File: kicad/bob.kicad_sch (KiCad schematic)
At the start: 53 parts, among them J1 Mini USB Female, J2 GPIO (Optional), J3 GPIO (Optional), J4 Battery Connector, J5 Conn_01x03_Male, SW1 Screw Switch, U1 W25Q64JVSS, U2 AMS1117-3.3, U3 RP2040, Y1 12MHz

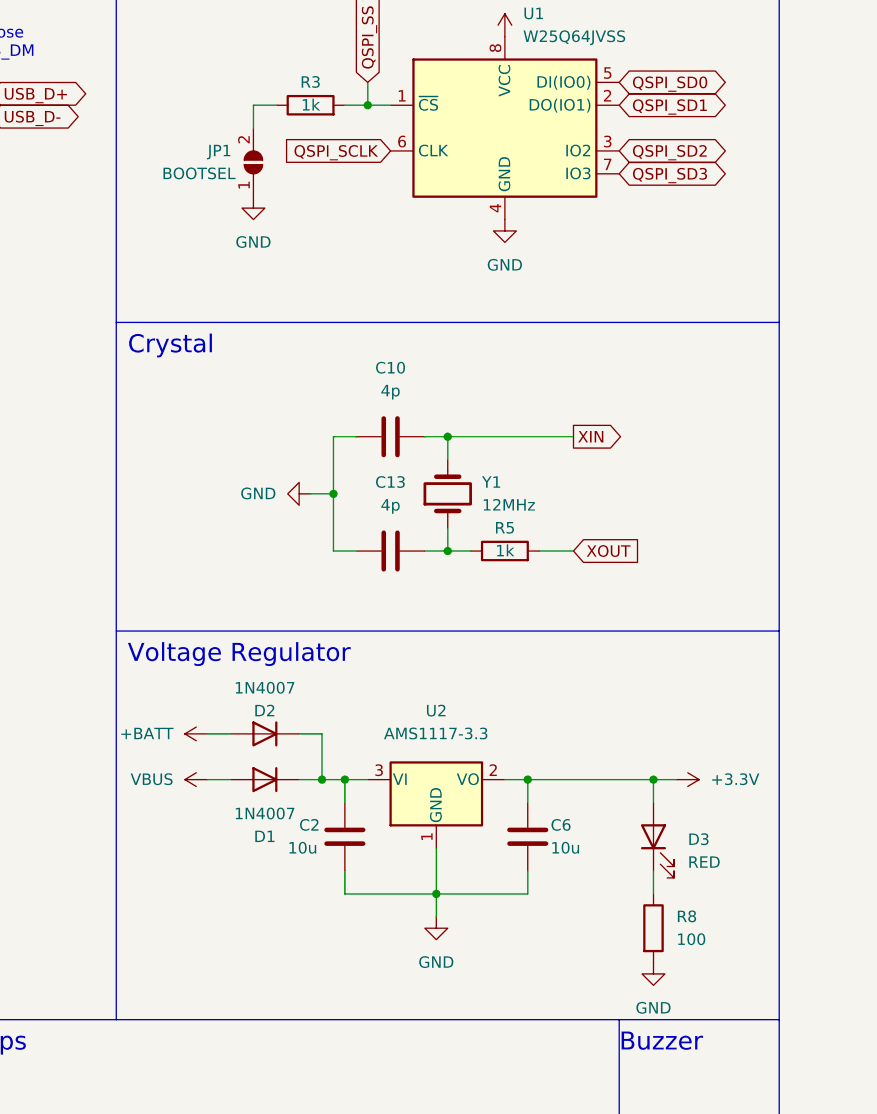
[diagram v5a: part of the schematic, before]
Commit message: Changed LED current limiter so it wont be so bright
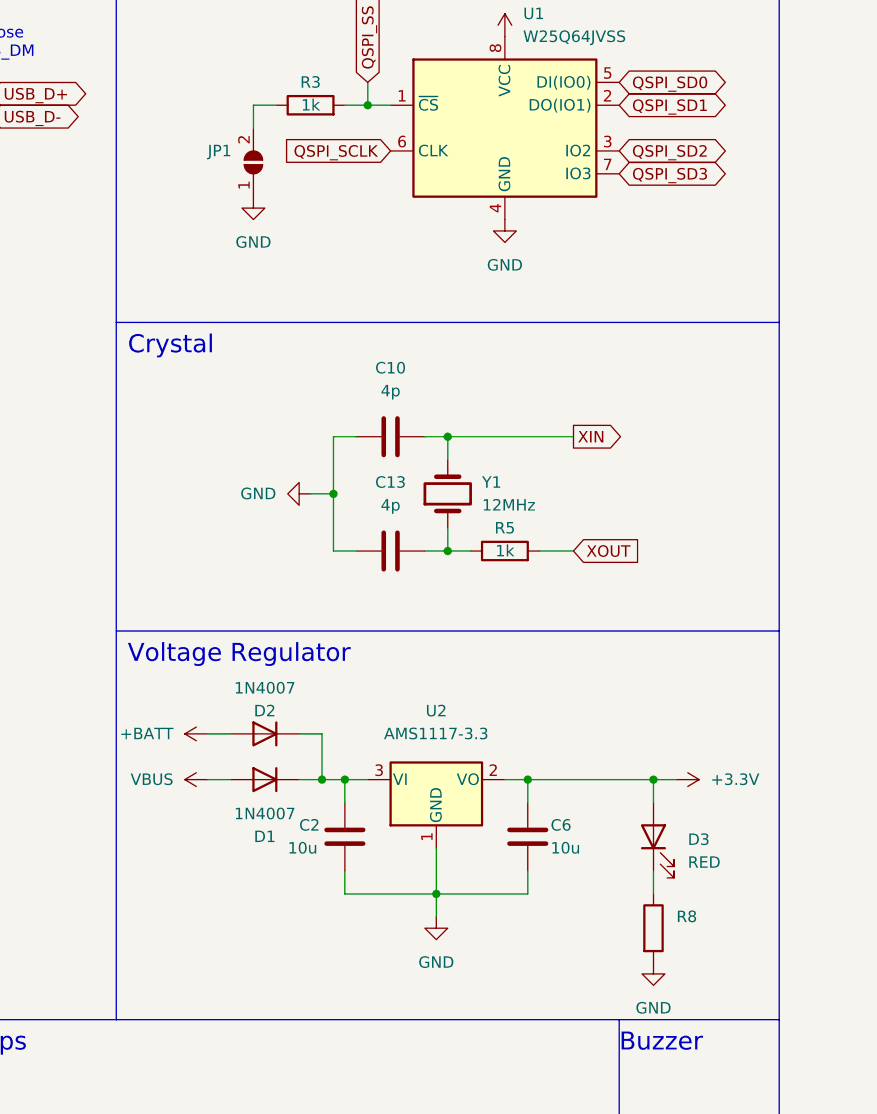
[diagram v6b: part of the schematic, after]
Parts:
- JP1: value BOOTSEL -> (none); footprint Jumper:SolderJumper-2_P1.3mm_Open_RoundedPad1.0x1.5mm -> (none)
- R8: value 100 -> (none)
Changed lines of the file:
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@@
   (symbol (lib_id "power:+3.3V") (at 247.65 27.94 0) (unit 1)
     (in_bom yes) (on_board yes) (fields_autoplaced)
-    (property "Reference" "#PWR?" (id 0) (at 247.65 31.75 0)
+    (property "Reference" "#PWR0106" (id 0) (at 247.65 31.75 0)
       (effects (font (size 1.27 1.27)) hide)
     )
@@
   (symbol (lib_id "power:GND") (at 261.62 40.64 90) (unit 1)
     (in_bom yes) (on_board yes) (fields_autoplaced)
-    (property "Reference" "#PWR?" (id 0) (at 267.97 40.64 0)
+    (property "Reference" "#PWR0149" (id 0) (at 267.97 40.64 0)
       (effects (font (size 1.27 1.27)) hide)
     )
@@
   (symbol (lib_id "power:+3.3V") (at 233.68 35.56 90) (unit 1)
     (in_bom yes) (on_board yes)
-    (property "Reference" "#PWR?" (id 0) (at 237.49 35.56 0)
+    (property "Reference" "#PWR0129" (id 0) (at 237.49 35.56 0)
       (effects (font (size 1.27 1.27)) hide)
     )
@@
   (symbol (lib_id "power:GND") (at 247.65 58.42 0) (unit 1)
     (in_bom yes) (on_board yes) (fields_autoplaced)
-    (property "Reference" "#PWR?" (id 0) (at 247.65 64.77 0)
+    (property "Reference" "#PWR0130" (id 0) (at 247.65 64.77 0)
       (effects (font (size 1.27 1.27)) hide)
     )
@@
       (effects (font (size 1.27 1.27)) (justify left))
     )
-    (property "Value" "100" (id 1) (at 184.15 126.9999 0)
+    (property "Value" "" (id 1) (at 184.15 126.9999 0)
       (effects (font (size 1.27 1.27)) (justify left))
     )
@@
   (symbol (lib_id "power:GND") (at 233.68 43.18 270) (unit 1)
     (in_bom yes) (on_board yes) (fields_autoplaced)
-    (property "Reference" "#PWR?" (id 0) (at 227.33 43.18 0)
+    (property "Reference" "#PWR0107" (id 0) (at 227.33 43.18 0)
       (effects (font (size 1.27 1.27)) hide)
     )
@@
       (effects (font (size 1.27 1.27)) (justify right))
     )
-    (property "Value" "BOOTSEL" (id 1) (at 127 41.91 90)
+    (property "Value" "" (id 1) (at 127 41.91 90)
       (effects (font (size 1.27 1.27)) (justify right))
     )
-    (property "Footprint" "Jumper:SolderJumper-2_P1.3mm_Open_RoundedPad1.0x1.5mm" (id 2) (at 137.16 40.64 0)
+    (property "Footprint" "" (id 2) (at 137.16 40.64 0)
       (effects (font (size 1.27 1.27)) hide)
     )
@@
   (symbol (lib_id "power:GND") (at 261.62 43.18 90) (unit 1)
     (in_bom yes) (on_board yes) (fields_autoplaced)
-    (property "Reference" "#PWR?" (id 0) (at 267.97 43.18 0)
+    (property "Reference" "#PWR0131" (id 0) (at 267.97 43.18 0)
       (effects (font (size 1.27 1.27)) hide)
     )
@@
       (reference "#PWR0105") (unit 1) (value "GND") (footprint "")
     )
+    (path "/22a21ef5-8d73-45f5-8c64-6674e766031d"
+      (reference "#PWR0106") (unit 1) (value "+3.3V") (footprint "")
+    )
+    (path "/adbdbf00-e19f-45aa-8793-9f170a1fa9e8"
+      (reference "#PWR0107") (unit 1) (value "GND") (footprint "")
+    )
     (path "/0029820e-80b7-4df3-ad7f-de6b7dce0bb1"
       (reference "#PWR0108") (unit 1) (value "GND") (footprint "")
@@
       (reference "#PWR0128") (unit 1) (value "+3.3V") (footprint "")
     )
+    (path "/8ff25ca3-7a6f-4ba9-9951-03e37d1c76eb"
+      (reference "#PWR0129") (unit 1) (value "+3.3V") (footprint "")
+    )
+    (path "/98a83e37-2266-4070-aae2-b4e3c95041c0"
+      (reference "#PWR0130") (unit 1) (value "GND") (footprint "")
+    )
+    (path "/f9ad9c73-d652-47d9-bade-657d8c1e1da7"
+      (reference "#PWR0131") (unit 1) (value "GND") (footprint "")
+    )
     (path "/81abba7b-65ef-4439-960f-9f1a27841048"
       (reference "#PWR0132") (unit 1) (value "GND") (footprint "")
@@
       (reference "#PWR0148") (unit 1) (value "GND") (footprint "")
     )
-    (path "/22a21ef5-8d73-45f5-8c64-6674e766031d"
-      (reference "#PWR?") (unit 1) (value "+3.3V") (footprint "")
-    )
     (path "/3868f898-270d-4a4f-a12d-011ac69fd79d"
-      (reference "#PWR?") (unit 1) (value "GND") (footprint "")
-    )
-    (path "/8ff25ca3-7a6f-4ba9-9951-03e37d1c76eb"
-      (reference "#PWR?") (unit 1) (value "+3.3V") (footprint "")
-    )
-    (path "/98a83e37-2266-4070-aae2-b4e3c95041c0"
-      (reference "#PWR?") (unit 1) (value "GND") (footprint "")
-    )
-    (path "/adbdbf00-e19f-45aa-8793-9f170a1fa9e8"
-      (reference "#PWR?") (unit 1) (value "GND") (footprint "")
-    )
-    (path "/f9ad9c73-d652-47d9-bade-657d8c1e1da7"
-      (reference "#PWR?") (unit 1) (value "GND") (footprint "")
+      (reference "#PWR0149") (unit 1) (value "GND") (footprint "")
     )
     (path "/e65ef186-5520-4142-8b10-d2898e4cdc2f"
@@
     )
     (path "/a20166e6-57cd-43ff-aad3-a0a7bed033c3"
-      (reference "R8") (unit 1) (value "100") (footprint "Resistor_SMD:R_0603_1608Metric")
+      (reference "R8") (unit 1) (value "220") (footprint "Resistor_SMD:R_0603_1608Metric")
     )
     (path "/6192c7bb-0335-4818-a72b-44407a15a4d1"
